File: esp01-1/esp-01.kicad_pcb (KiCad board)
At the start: 2 copper layers, 64.1 x 46.7 mm, 23 parts, among them P1 USB_B, SW1 Reset, SW2 Bootloader, U1 ESP-01V090, U2 LT1761-3.3, U3 MCP2200, Y1 CRYSTAL_SMD

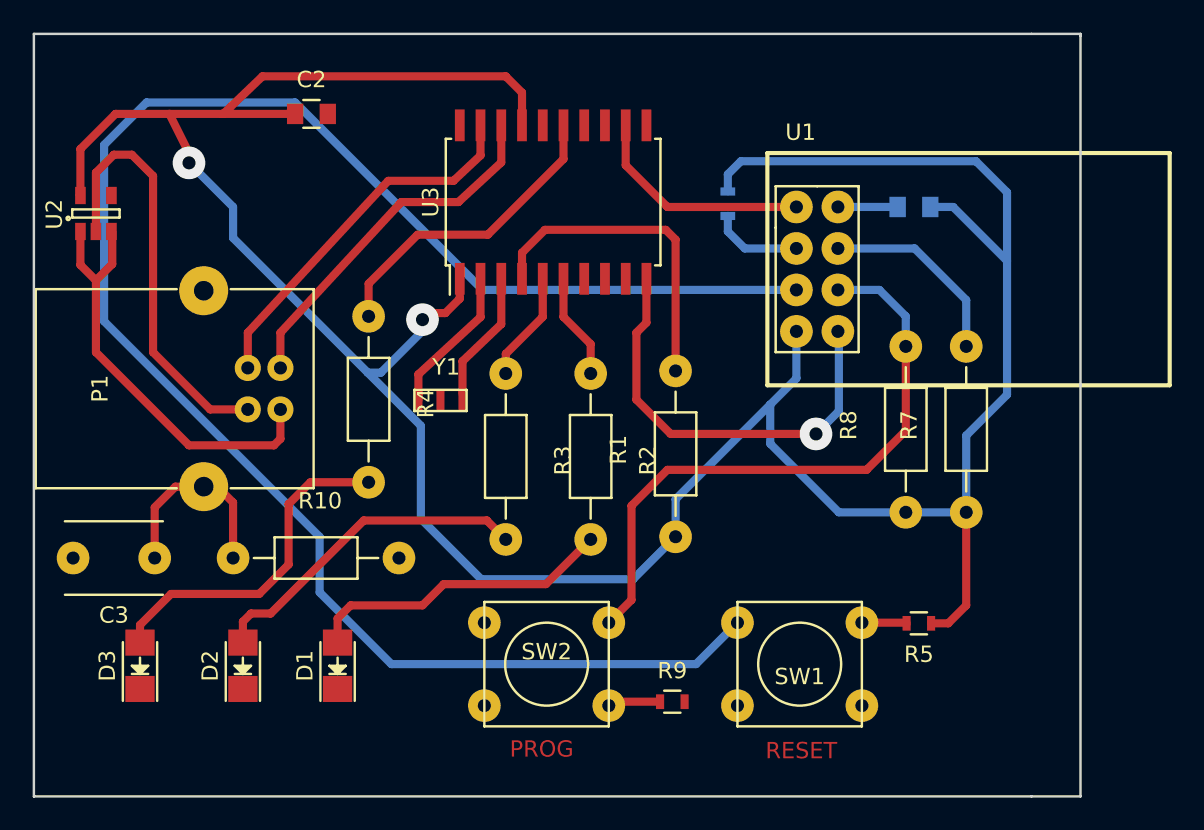
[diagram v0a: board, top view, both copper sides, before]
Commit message: Fixed design error. The USB ocnnector can only be soldered the background
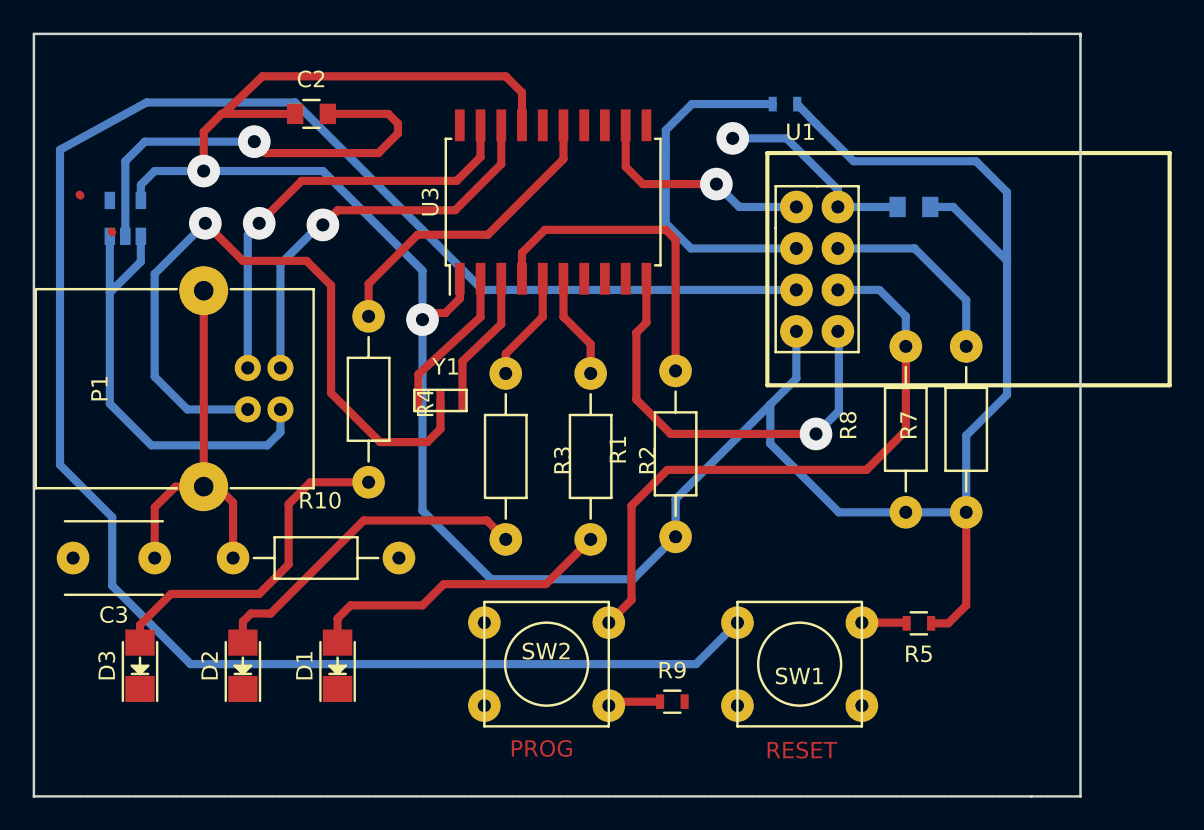
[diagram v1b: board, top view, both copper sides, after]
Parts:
- U2: moved to B.Cu
- moved R6 7.03 mm to (118.2, 195.9), turned to 0 degrees
- moved U2 1.82 mm to (77.8, 202.9)
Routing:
- net GND: track 29.8 -> 83.5 mm, vias 0 -> 3
- net Net-(R6-Pad1): track 5.58 -> 21.6 mm
- net +3V3: track 183.3 -> 170.4 mm
- net Net-(C3-Pad1): track 12.2 -> 24.2 mm
- net Net-(R5-Pad2): track 112.3 -> 122.7 mm
- net /USBD+: track 23.5 -> 26.3 mm, vias 0 -> 1
- net /USBD-: track 22.8 -> 24.8 mm, vias 0 -> 1
- net +5V: track 26.9 -> 27.7 mm
- net Net-(U1-Pad1): vias 0 -> 1

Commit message: Added a big decoupling capacitor because of the ESP current glutony
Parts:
- added C4: 150uF, Capacitors_SMD:C_1210_HandSoldering, F.Cu at (129.3, 228.2)
- moved R5 11.6 mm to (115.3, 224.2), turned to 270 degrees
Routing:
- net +3V3: track 170.4 -> 171.6 mm
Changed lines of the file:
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@@
 (kicad_pcb (version 4) (host pcbnew 4.0.4+e1-6308~48~ubuntu14.04.1-stable)
   (general
-    (links 52)
+    (links 54)
     (no_connects 3)
-    (area 65.5 185.3 146.6 246)
+    (area 72.124999 191.524999 136.375001 238.375001)
     (thickness 1.6)
     (drawings 13)
-    (tracks 199)
+    (tracks 197)
     (zones 0)
-    (modules 23)
+    (modules 24)
     (nets 31)
   )
@@
     (visible_elements 7FFFFFFF)
     (pcbplotparams
-      (layerselection 0x01000_80000001)
+      (layerselection 0x01000_00000001)
       (usegerberextensions false)
       (excludeedgelayer true)
       (linewidth 0.150000)
-      (plotframeref true)
+      (plotframeref false)
       (viasonmask false)
       (mode 1)
@@
       (psnegative false)
       (psa4output false)
-      (plotreference true)
-      (plotvalue true)
+      (plotreference false)
+      (plotvalue false)
       (plotinvisibletext false)
       (padsonsilk false)
       (subtractmaskfromsilk false)
       (outputformat 5)
-      (mirror false)
+      (mirror true)
       (drillshape 2)
       (scaleselection 1)
@@
   )
   (module Resistors_SMD:R_0603 (layer F.Cu)
-    (at 126.4 227.7 180)
+    (at 115.3 224.2 270)
     (descr "Resistor SMD 0603, reflow soldering, Vishay (see dcrcw.pdf)")
     (tags "resistor 0603")
     (attr smd)
-    (fp_text reference R5 (at 0 -1.9 180) (layer F.SilkS)
-      (effects (font (size 1 1) (thickness 0.15)))
-    )
-    (fp_text value 10K (at 0 1.9 180) (layer F.Fab)
+    (fp_text reference R5 (at 0 -1.9 270) (layer F.SilkS)
+      (effects (font (size 1 1) (thickness 0.15)))
+    )
+    (fp_text value 10K (at 0 1.9 270) (layer F.Fab)
       (effects (font (size 1 1) (thickness 0.15)))
     )
@@
     (fp_line (start 0.5 0.675) (end -0.5 0.675) (layer F.SilkS) (width 0.15))
     (fp_line (start -0.5 -0.675) (end 0.5 -0.675) (layer F.SilkS) (width 0.15))
-    (pad 1 smd rect (at -0.75 0 180) (size 0.5 0.9) (layers F.Cu F.Paste F.Mask)
+    (pad 1 smd rect (at -0.75 0 270) (size 0.5 0.9) (layers F.Cu F.Paste F.Mask)
       (net 6 +3V3))
-    (pad 2 smd rect (at 0.75 0 180) (size 0.5 0.9) (layers F.Cu F.Paste F.Mask)
+    (pad 2 smd rect (at 0.75 0 270) (size 0.5 0.9) (layers F.Cu F.Paste F.Mask)
       (net 18 "Net-(R5-Pad2)"))
     (model Resistors_SMD.3dshapes/R_0603.wrl
@@
       (net 21 "Net-(U3-Pad2)"))
   )
+  (module Capacitors_SMD:C_1210_HandSoldering (layer F.Cu)
+    (at 129.3 228.2 270)
+    (descr "Capacitor SMD 1210, hand soldering")
+    (tags "capacitor 1210")
+    (attr smd)
+    (fp_text reference C4 (at 0 -2.7 270) (layer F.SilkS)
+      (effects (font (size 1 1) (thickness 0.15)))
+    )
+    (fp_text value 150uF (at 0 2.7 270) (layer F.Fab)
+      (effects (font (size 1 1) (thickness 0.15)))
+    )
+    (fp_line (start -1.6 1.25) (end -1.6 -1.25) (layer F.Fab) (width 0.15))
+    (fp_line (start 1.6 1.25) (end -1.6 1.25) (layer F.Fab) (width 0.15))
+    (fp_line (start 1.6 -1.25) (end 1.6 1.25) (layer F.Fab) (width 0.15))
+    (fp_line (start -1.6 -1.25) (end 1.6 -1.25) (layer F.Fab) (width 0.15))
+    (fp_line (start -3.3 -1.6) (end 3.3 -1.6) (layer F.CrtYd) (width 0.05))
+    (fp_line (start -3.3 1.6) (end 3.3 1.6) (layer F.CrtYd) (width 0.05))
+    (fp_line (start -3.3 -1.6) (end -3.3 1.6) (layer F.CrtYd) (width 0.05))
+    (fp_line (start 3.3 -1.6) (end 3.3 1.6) (layer F.CrtYd) (width 0.05))
+    (fp_line (start 1 -1.475) (end -1 -1.475) (layer F.SilkS) (width 0.15))
+    (fp_line (start -1 1.475) (end 1 1.475) (layer F.SilkS) (width 0.15))
+    (pad 1 smd rect (at -2 0 270) (size 2 2.5) (layers F.Cu F.Paste F.Mask)
+      (net 6 +3V3))
+    (pad 2 smd rect (at 2 0 270) (size 2 2.5) (layers F.Cu F.Paste F.Mask)
+      (net 2 GND))
+    (model Capacitors_SMD.3dshapes/C_1210_HandSoldering.wrl
+      (at (xyz 0 0 0))
+      (scale (xyz 1 1 1))
+      (rotate (xyz 0 0 0))
+    )
+  )
   (target plus (at 144.1 243.3) (size 5) (width 0.15) (layer Edge.Cuts))
   (target plus (at 69 243.5) (size 5) (width 0.15) (layer Edge.Cuts))
@@
   (gr_line (start 72.2 238.3) (end 72.2 191.6) (angle 90) (layer Edge.Cuts) (width 0.15))
   (gr_line (start 136.3 191.7) (end 136.3 238.3) (angle 90) (layer Edge.Cuts) (width 0.15))
-  (segment (start 75 201.45) (end 75.05 201.5) (width 0.5) (layer F.Cu) (net 0))
-  (segment (start 77 203.75) (end 76.95 203.7) (width 0.5) (layer F.Cu) (net 0))
   (segment (start 108.445 197.2) (end 108.445 199.745) (width 0.5) (layer F.Cu) (net 1))
   (segment (start 115.4 202.2) (end 118.9 202.2) (width 0.5) (layer B.Cu) (net 1))
@@
   (segment (start 109.5 200.8) (end 114 200.8) (width 0.5) (layer F.Cu) (net 1))
   (segment (start 108.445 199.745) (end 109.5 200.8) (width 0.5) (layer F.Cu) (net 1))
-  (segment (start 121.44 202.2) (end 121.44 201.14) (width 0.5) (layer B.Cu) (net 2) (status 400000))
+  (segment (start 121.44 202.2) (end 121.44 201.14) (width 0.5) (layer B.Cu) (net 2))
   (segment (start 114.9 197.9) (end 114.8 197.9) (width 0.5) (layer F.Cu) (net 2))
   (segment (start 115 198) (end 114.9 197.9) (width 0.5) (layer F.Cu) (net 2))
@@
   (segment (start 121.44 202.2) (end 125.1 202.2) (width 0.5) (layer B.Cu) (net 2))
   (segment (start 110.9 198.8) (end 110.9 197.5) (width 0.5) (layer B.Cu) (net 3))
-  (segment (start 112.5 195.9) (end 117.45 195.9) (width 0.5) (layer B.Cu) (net 3) (status 800000))
+  (segment (start 112.5 195.9) (end 117.45 195.9) (width 0.5) (layer B.Cu) (net 3))
   (segment (start 110.9 197.5) (end 112.5 195.9) (width 0.5) (layer B.Cu) (net 3))
   (segment (start 112.44 204.74) (end 118.9 204.74) (width 0.5) (layer B.Cu) (net 3))
@@
   (segment (start 123.2 218.3) (end 111 218.3) (width 0.5) (layer F.Cu) (net 5))
   (segment (start 125.6 215.9) (end 123.2 218.3) (width 0.5) (layer F.Cu) (net 5))
+  (segment (start 129.3 220.9) (end 129.3 226.2) (width 0.5) (layer F.Cu) (net 6))
+  (segment (start 111.5 222.4) (end 114.25 222.4) (width 0.5) (layer F.Cu) (net 6))
+  (segment (start 114.25 222.4) (end 115.3 223.45) (width 0.5) (layer F.Cu) (net 6))
   (segment (start 118.95 195.9) (end 120.1 197.1) (width 0.5) (layer B.Cu) (net 6) (status 10))
   (segment (start 120.1 197.1) (end 122.4 199.4) (width 0.5) (layer B.Cu) (net 6))
@@
   (segment (start 117.3 214.3) (end 118.9 212.7) (width 0.5) (layer B.Cu) (net 6))
   (segment (start 118.9 212.7) (end 118.9 209.82) (width 0.5) (layer B.Cu) (net 6))
-  (segment (start 127.15 227.7) (end 128.2 227.7) (width 0.5) (layer F.Cu) (net 6))
-  (segment (start 129.3 226.6) (end 129.3 220.9) (width 0.5) (layer F.Cu) (net 6))
-  (segment (start 128.2 227.7) (end 129.3 226.6) (width 0.5) (layer F.Cu) (net 6))
   (segment (start 129.4 220.6) (end 129.3 220.5) (width 0.5) (layer F.Cu) (net 6))
   (segment (start 98.285 207.815) (end 98.285 206.6) (width 0.5) (layer F.Cu) (net 6))
@@
   (segment (start 95.7 203.9) (end 100 203.9) (width 0.5) (layer F.Cu) (net 17))
   (segment (start 92.7 206.9) (end 95.7 203.9) (width 0.5) (layer F.Cu) (net 17))
+  (segment (start 115.3 224.95) (end 115.3 227.65) (width 0.5) (layer F.Cu) (net 18))
+  (segment (start 115.3 227.65) (end 115.29 227.66) (width 0.5) (layer F.Cu) (net 18))
   (segment (start 73.8 209.5) (end 73.8 218) (width 0.5) (layer B.Cu) (net 18))
   (segment (start 81.8 230.2) (end 95.7 230.2) (width 0.5) (layer B.Cu) (net 18))
@@
   (segment (start 88.2 195.8) (end 79.1 195.8) (width 0.5) (layer B.Cu) (net 18))
   (segment (start 99.68 207.28) (end 88.2 195.8) (width 0.5) (layer B.Cu) (net 18))
-  (segment (start 122.91 227.66) (end 125.61 227.66) (width 0.5) (layer F.Cu) (net 18))
-  (segment (start 125.61 227.66) (end 125.65 227.7) (width 0.5) (layer F.Cu) (net 18))
   (segment (start 107.65 232.5) (end 107.41 232.74) (width 0.5) (layer F.Cu) (net 19))
   (segment (start 110.55 232.5) (end 107.65 232.5) (width 0.5) (layer F.Cu) (net 19))

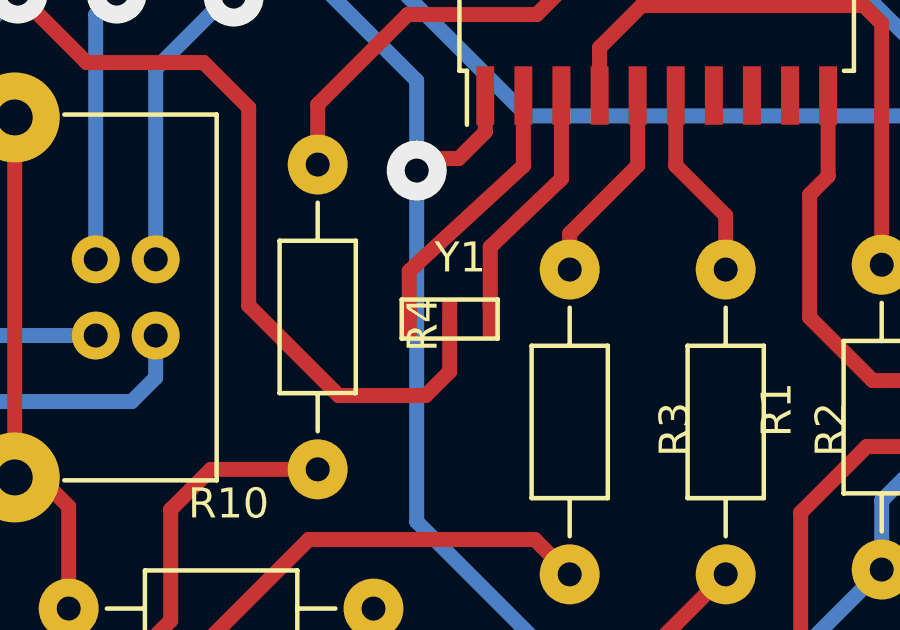
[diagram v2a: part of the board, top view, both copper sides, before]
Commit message: Updated project to follow the kicad official libraries evolutions
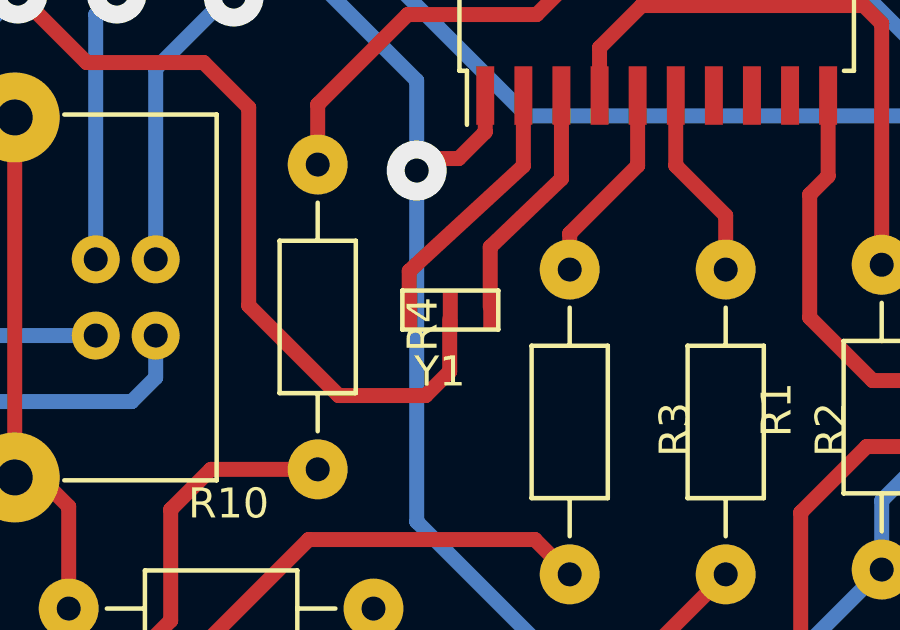
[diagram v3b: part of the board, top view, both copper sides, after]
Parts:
- moved Y1 3.37 mm to (98.7, 214.4), turned to 180 degrees
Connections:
- Y1 pad 1: Net-(U3-Pad2) -> Net-(U3-Pad3)
- Y1 pad 3: Net-(U3-Pad3) -> Net-(U3-Pad2)
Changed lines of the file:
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@@
-(kicad_pcb (version 4) (host pcbnew 4.0.4+e1-6308~48~ubuntu14.04.1-stable)
+(kicad_pcb (version 4) (host pcbnew 4.0.6-e0-6349~53~ubuntu14.04.1)
   (general
     (links 54)
@@
   )
   (module cdtx:Resonator_3.2x1.3mm (layer F.Cu)
-    (at 95.5 213.4)
-    (fp_text reference Y1 (at 1.95 -1.4) (layer F.SilkS)
-      (effects (font (size 1 1) (thickness 0.15)))
-    )
-    (fp_text value CRYSTAL_SMD (at 1.15 3.25) (layer F.Fab)
+    (at 98.72 214.4 180)
+    (fp_text reference Y1 (at 1.95 -1.4 180) (layer F.SilkS)
+      (effects (font (size 1 1) (thickness 0.15)))
+    )
+    (fp_text value CRYSTAL_SMD (at 1.15 3.25 180) (layer F.Fab)
       (effects (font (size 1 1) (thickness 0.15)))
     )
@@
     (fp_line (start 3.2 1.3) (end 0 1.3) (layer F.SilkS) (width 0.15))
     (fp_line (start 0 1.3) (end 0 0) (layer F.SilkS) (width 0.15))
-    (pad 3 smd rect (at 2.95 0.65) (size 0.5 1.3) (layers F.Cu F.Paste F.Mask)
+    (pad 3 smd rect (at 2.95 0.65 180) (size 0.5 1.3) (layers F.Cu F.Paste F.Mask)
+      (net 21 "Net-(U3-Pad2)"))
+    (pad 2 smd rect (at 1.6 0.65 180) (size 0.5 1.3) (layers F.Cu F.Paste F.Mask)
+      (net 2 GND))
+    (pad 1 smd rect (at 0.25 0.65 180) (size 0.5 1.3) (layers F.Cu F.Paste F.Mask)
       (net 22 "Net-(U3-Pad3)"))
-    (pad 2 smd rect (at 1.6 0.65) (size 0.5 1.3) (layers F.Cu F.Paste F.Mask)
-      (net 2 GND))
-    (pad 1 smd rect (at 0.25 0.65) (size 0.5 1.3) (layers F.Cu F.Paste F.Mask)
-      (net 21 "Net-(U3-Pad2)"))
   )
   (module Capacitors_SMD:C_1210_HandSoldering (layer F.Cu)
@@
   (segment (start 121.44 201.14) (end 118.3 198) (width 0.5) (layer B.Cu) (net 2))
   (segment (start 85.30102 214.6) (end 81.6 214.6) (width 0.5) (layer B.Cu) (net 2))
-  (segment (start 97.1 215.8) (end 97.1 214.05) (width 0.5) (layer F.Cu) (net 2))
+  (segment (start 97.1 215.8) (end 97.1 214.05) (width 0.5) (layer F.Cu) (net 2) (status 20))
   (segment (start 96.3 216.6) (end 97.1 215.8) (width 0.5) (layer F.Cu) (net 2))
   (segment (start 93.4 216.6) (end 96.3 216.6) (width 0.5) (layer F.Cu) (net 2))
@@
   (segment (start 107.65 232.5) (end 107.41 232.74) (width 0.5) (layer F.Cu) (net 19))
   (segment (start 110.55 232.5) (end 107.65 232.5) (width 0.5) (layer F.Cu) (net 19))
-  (segment (start 95.75 214.05) (end 95.75 212.45) (width 0.5) (layer F.Cu) (net 21) (status 10))
   (segment (start 99.555 208.945) (end 99.555 206.6) (width 0.5) (layer F.Cu) (net 21))
   (segment (start 95.75 212.45) (end 99.555 208.945) (width 0.5) (layer F.Cu) (net 21))
+  (segment (start 95.75 214.05) (end 95.75 212.45) (width 0.5) (layer F.Cu) (net 21) (status 10))
   (segment (start 98.45 213.65) (end 98.45 211.65) (width 0.5) (layer F.Cu) (net 22) (status 10))
+  (segment (start 98.45 211.65) (end 100.825 209.375) (width 0.5) (layer F.Cu) (net 22))
   (segment (start 100.825 209.375) (end 100.825 206.6) (width 0.5) (layer F.Cu) (net 22))
-  (segment (start 98.45 211.65) (end 100.825 209.375) (width 0.5) (layer F.Cu) (net 22))
   (segment (start 82.601 207.33052) (end 82.601 219.32948) (width 0.5) (layer F.Cu) (net 30))
   (segment (start 84.4 223.7) (end 84.4 220.3) (width 0.5) (layer F.Cu) (net 30))
